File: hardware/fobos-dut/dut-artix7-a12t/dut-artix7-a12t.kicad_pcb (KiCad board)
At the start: 2 copper layers, 67 parts, among them J1 Target, J3 Vcore, J5 Conn_01x02, Q1 FDS9435A, U1 XC7A12T-CSG325, U2 SP3003-04ATG, U3 SP3003-04ATG, U4 SP3003-04ATG, U5 INA225, U6 BGA2801, U7 W25Q32JVSS

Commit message: updated 3d model path of sma connector
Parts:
- added J4: Glitch, cerg:SMA-JOHNSON-142-0701-801, F.Cu at (-147.3, 152.7)
- added J6: Measure, cerg:SMA-JOHNSON-142-0701-801, F.Cu at (-125.5, 152.4)
- moved J1 24.1 mm to (-155.7, 194.8), turned to 180 degrees
- moved U1 11.3 mm to (-97.3, 165.1)

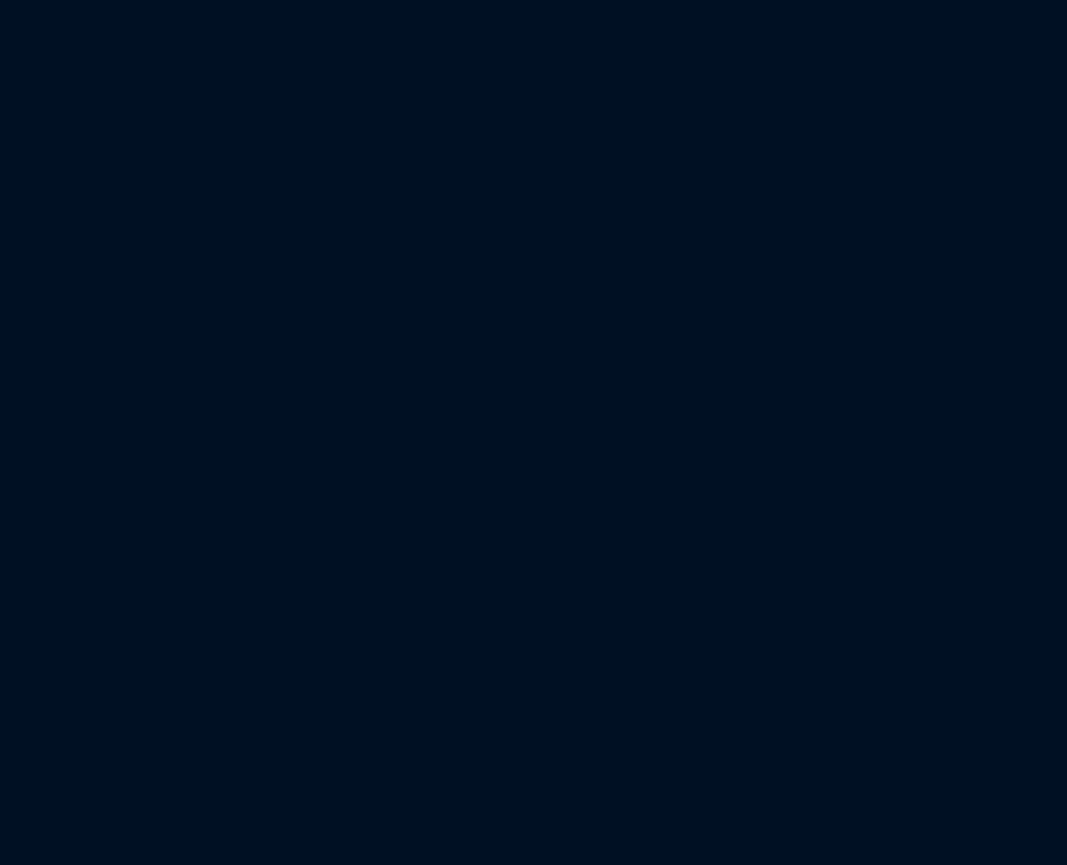
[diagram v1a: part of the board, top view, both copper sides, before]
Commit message: Finished the LTC3659 circuit - added gnd, epad to gnd net Completed PGOOD LED circuit Added slide switch to serve as ON_OFF switch
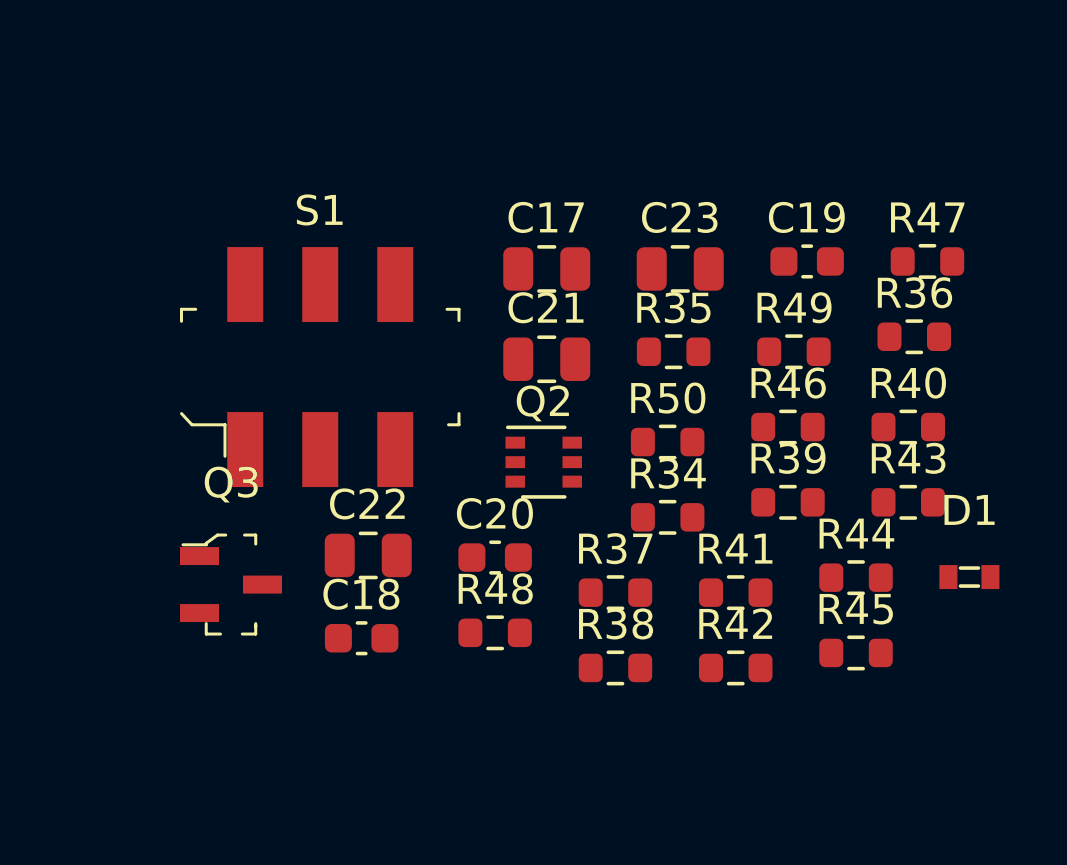
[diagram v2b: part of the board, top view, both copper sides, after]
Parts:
- added C17: 22uF, Capacitor_SMD:C_0805_2012Metric, F.Cu at (-58.3, 198.5)
- added C18: 20pF, Capacitor_SMD:C_0603_1608Metric, F.Cu at (-64.5, 210.8)
- added C19: 20pF, Capacitor_SMD:C_0603_1608Metric, F.Cu at (-49.6, 198.2)
- added C20: 20pF, Capacitor_SMD:C_0603_1608Metric, F.Cu at (-60.0, 208.1)
- added C21: 22uF, Capacitor_SMD:C_0805_2012Metric, F.Cu at (-58.3, 201.5)
- added C22: 10uF, Capacitor_SMD:C_0805_2012Metric, F.Cu at (-64.2, 208.1)
- added C23: 10uF, Capacitor_SMD:C_0805_2012Metric, F.Cu at (-53.9, 198.5)
- added D1: LG_L29K-G2J1-24-Z, digikey-footprints:0603, F.Cu at (-44.2, 208.8)
- added Q2: MBT3904DW1, Package_TO_SOT_SMD:SOT-363_SC-70-6, F.Cu at (-58.4, 204.9)
- added Q3: FDV301N, digikey-footprints:SOT-23-3, F.Cu at (-68.8, 209.0)
- added R34: 3.48KR, Resistor_SMD:R_0603_1608Metric, F.Cu at (-54.3, 206.8)
- added R35: 10KR, Resistor_SMD:R_0603_1608Metric, F.Cu at (-54.1, 201.3)
- added R36: 1KR, Resistor_SMD:R_0603_1608Metric, F.Cu at (-46.0, 200.8)
- added R37: 0, Resistor_SMD:R_0603_1608Metric, F.Cu at (-56.0, 209.3)
- added R38: 100KR, Resistor_SMD:R_0603_1608Metric, F.Cu at (-56.0, 211.8)
- added R39: 100KR, Resistor_SMD:R_0603_1608Metric, F.Cu at (-50.3, 206.3)
- added R40: 100KR, Resistor_SMD:R_0603_1608Metric, F.Cu at (-46.2, 203.8)
- added R41: 4.7KR, Resistor_SMD:R_0603_1608Metric, F.Cu at (-52.0, 209.3)
- added R42: 10KR, Resistor_SMD:R_0603_1608Metric, F.Cu at (-52.0, 211.8)
- added R43: 10KR, Resistor_SMD:R_0603_1608Metric, F.Cu at (-46.2, 206.3)
- added R44: 10KR, Resistor_SMD:R_0603_1608Metric, F.Cu at (-48.0, 208.8)
- added R45: 10KR, Resistor_SMD:R_0603_1608Metric, F.Cu at (-48.0, 211.3)
- added R46: 120KR, Resistor_SMD:R_0603_1608Metric, F.Cu at (-50.3, 203.8)
- added R47: 120KR, Resistor_SMD:R_0603_1608Metric, F.Cu at (-45.6, 198.2)
- added R48: 57.6KR, Resistor_SMD:R_0603_1608Metric, F.Cu at (-60.0, 210.6)
- added R49: 100KR, Resistor_SMD:R_0603_1608Metric, F.Cu at (-50.1, 201.3)
- added R50: 800R, Resistor_SMD:R_0603_1608Metric, F.Cu at (-54.3, 204.3)
- added S1: JS202011SCQN, digikey-footprints:Switch_Slide_JS202011SCQN, F.Cu at (-65.8, 201.8)

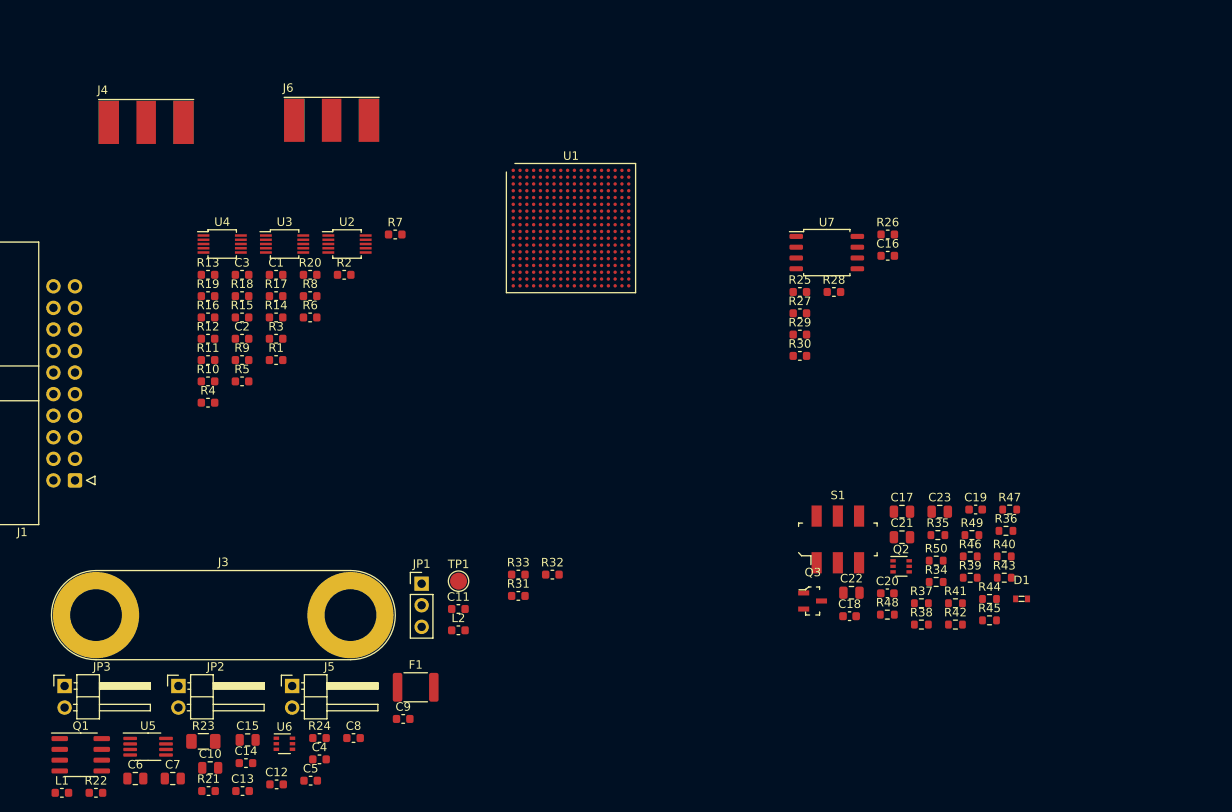
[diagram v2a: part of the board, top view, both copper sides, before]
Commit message: -Added TS3A27518EIPWRQ1 6 circuit analog SPDT switch -Connected tripple output power supply to FPGA power pins -Added bypass and decoupling capacitors to the FPGA power pins(these will be DNP) -Swapped out the old bulky banana jack socket parts for 1050752001 and 1050753001 -Added JTAG header -Added test loops -Added boot mode dip switch -Swapped out the right angle 0.1" headers for vertical 0.1" headers(personal preference) -Working my way through the 7_series_schematic_review_recommendations spreadsheet
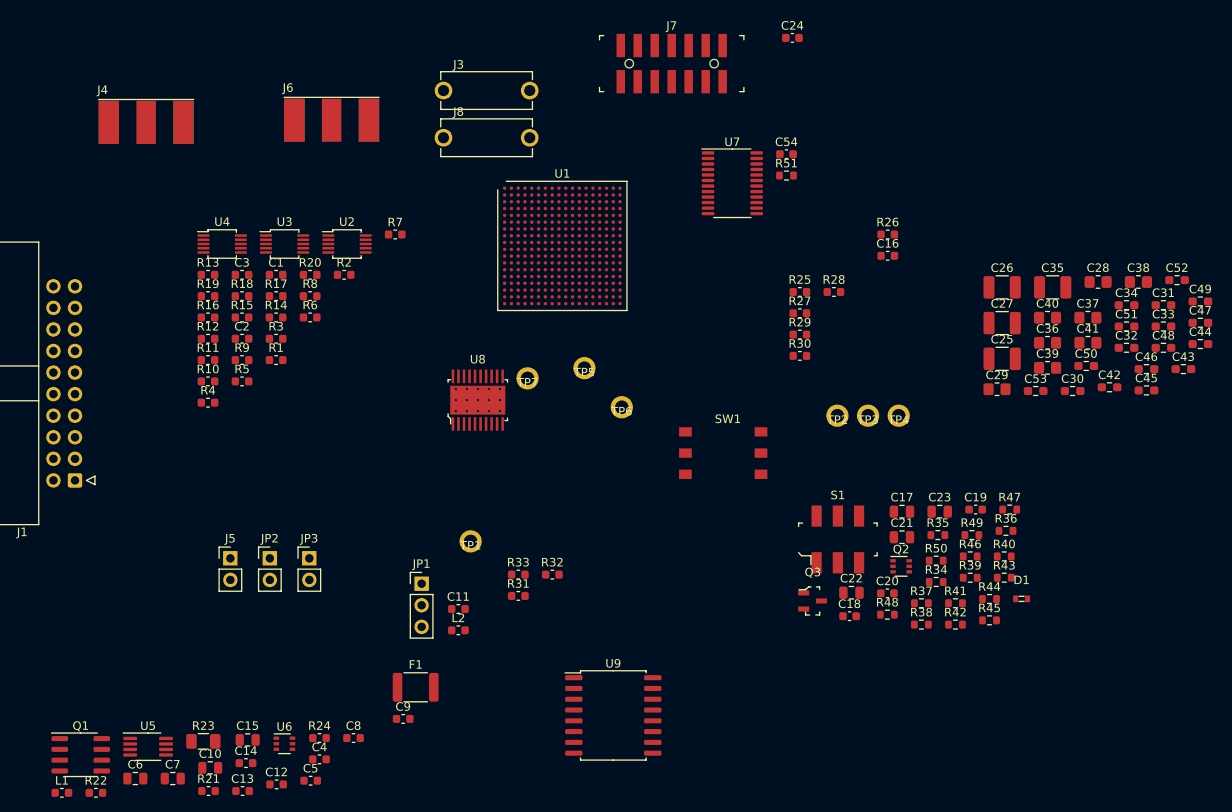
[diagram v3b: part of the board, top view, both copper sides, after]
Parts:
- added C24: 100nF, Capacitor_SMD:C_0603_1608Metric, F.Cu at (-71.2, 142.7)
- added C25: 100uF, Resistor_SMD:R_1210_3225Metric_Pad1.30x2.65mm_HandSolder, F.Cu at (-46.5, 180.5)
- added C26: 47uF, Resistor_SMD:R_1210_3225Metric_Pad1.30x2.65mm_HandSolder, F.Cu at (-46.5, 172.1)
- added C27: 47uF, Resistor_SMD:R_1210_3225Metric_Pad1.30x2.65mm_HandSolder, F.Cu at (-46.5, 176.3)
- added C28: 4.7uF, Resistor_SMD:R_0805_2012Metric_Pad1.20x1.40mm_HandSolder, F.Cu at (-35.2, 171.4)
- added C29: 4.7uF, Resistor_SMD:R_0805_2012Metric_Pad1.20x1.40mm_HandSolder, F.Cu at (-47.1, 184.1)
- added C30: .47uF, Resistor_SMD:R_0603_1608Metric_Pad0.98x0.95mm_HandSolder, F.Cu at (-38.2, 184.3)
- added C31: .47uF, Resistor_SMD:R_0603_1608Metric_Pad0.98x0.95mm_HandSolder, F.Cu at (-27.5, 174.2)
- added C32: .47uF, Resistor_SMD:R_0603_1608Metric_Pad0.98x0.95mm_HandSolder, F.Cu at (-31.9, 179.2)
- added C33: .47uF, Resistor_SMD:R_0603_1608Metric_Pad0.98x0.95mm_HandSolder, F.Cu at (-27.5, 176.7)
- added C34: .47uF, Resistor_SMD:R_0603_1608Metric_Pad0.98x0.95mm_HandSolder, F.Cu at (-31.9, 174.2)
- added C35: 47uF, Resistor_SMD:R_1210_3225Metric_Pad1.30x2.65mm_HandSolder, F.Cu at (-40.5, 172.1)
- added C36: 4.7uF, Resistor_SMD:R_0805_2012Metric_Pad1.20x1.40mm_HandSolder, F.Cu at (-41.1, 178.6)
- added C37: 4.7uF, Resistor_SMD:R_0805_2012Metric_Pad1.20x1.40mm_HandSolder, F.Cu at (-36.4, 175.7)
- added C38: 4.7uF, Resistor_SMD:R_0805_2012Metric_Pad1.20x1.40mm_HandSolder, F.Cu at (-30.4, 171.4)
- added C39: 4.7uF, Resistor_SMD:R_0805_2012Metric_Pad1.20x1.40mm_HandSolder, F.Cu at (-41.1, 181.6)
- added C40: 4.7uF, Resistor_SMD:R_0805_2012Metric_Pad1.20x1.40mm_HandSolder, F.Cu at (-41.1, 175.7)
- added C41: 4.7uF, Resistor_SMD:R_0805_2012Metric_Pad1.20x1.40mm_HandSolder, F.Cu at (-36.4, 178.6)
- added C42: .47uF, Resistor_SMD:R_0603_1608Metric_Pad0.98x0.95mm_HandSolder, F.Cu at (-33.9, 183.8)
- added C43: .47uF, Resistor_SMD:R_0603_1608Metric_Pad0.98x0.95mm_HandSolder, F.Cu at (-25.1, 181.7)
- added C44: .47uF, Resistor_SMD:R_0603_1608Metric_Pad0.98x0.95mm_HandSolder, F.Cu at (-23.1, 178.8)
- added C45: .47uF, Resistor_SMD:R_0603_1608Metric_Pad0.98x0.95mm_HandSolder, F.Cu at (-29.5, 184.2)
- added C46: .47uF, Resistor_SMD:R_0603_1608Metric_Pad0.98x0.95mm_HandSolder, F.Cu at (-29.5, 181.7)
- added C47: .47uF, Resistor_SMD:R_0603_1608Metric_Pad0.98x0.95mm_HandSolder, F.Cu at (-23.1, 176.2)
- added C48: .47uF, Resistor_SMD:R_0603_1608Metric_Pad0.98x0.95mm_HandSolder, F.Cu at (-27.5, 179.2)
- added C49: .47uF, Resistor_SMD:R_0603_1608Metric_Pad0.98x0.95mm_HandSolder, F.Cu at (-23.1, 173.7)
- added C50: .47uF, Resistor_SMD:R_0603_1608Metric_Pad0.98x0.95mm_HandSolder, F.Cu at (-36.6, 181.3)
- added C51: .47uF, Resistor_SMD:R_0603_1608Metric_Pad0.98x0.95mm_HandSolder, F.Cu at (-31.9, 176.7)
- added C52: .47uF, Resistor_SMD:R_0603_1608Metric_Pad0.98x0.95mm_HandSolder, F.Cu at (-25.9, 171.2)
- added C53: .47uF, Resistor_SMD:R_0603_1608Metric_Pad0.98x0.95mm_HandSolder, F.Cu at (-42.5, 184.3)
- added C54: 100nF, Capacitor_SMD:C_0603_1608Metric, F.Cu at (-71.9, 156.4)
- added J7: 0878321420, digikey-footprints:PinHeader_2x7_P2mm_SMD, F.Cu at (-85.4, 145.7)
- added J8: 1050752001, cerg:105075X001, F.Cu at (-112.3, 154.5)
- added R51: 10KR, Resistor_SMD:R_0603_1608Metric, F.Cu at (-71.9, 158.9)
- added SW1: SW_DIP_x03, cerg:DS04-254-2-03BK-SMT, F.Cu at (-83.8, 189.1)
- added TP2: 5281, cerg:5281, F.Cu at (-65.9, 187.2)
- added TP3: 5281, cerg:5281, F.Cu at (-62.3, 187.2)
- added TP4: 5281, cerg:5281, F.Cu at (-58.7, 187.2)
- added TP5: 5281, cerg:5281, F.Cu at (-95.7, 181.6)
- added TP6: 5281, cerg:5281, F.Cu at (-91.3, 186.2)
- added TP7: 5281, cerg:5281, F.Cu at (-102.4, 182.8)
- added U8: LTC3569EFE#PBF, digikey-footprints:TSSOP-20-1EP_W4.4mm, F.Cu at (-108.3, 185.4)
- added U9: IS25LP256D-JMLE, Package_SO:SOIC-16W_7.5x10.3mm_P1.27mm, F.Cu at (-92.3, 222.5)
- J3: value Vcore -> 1050753001; footprint Connector:Banana_Jack_2Pin -> cerg:105075X001
- J5, JP2, JP3: footprint Connector_PinHeader_2.54mm:PinHeader_1x02_P2.54mm_Horizontal -> Connector_PinHeader_2.54mm:PinHeader_1x02_P2.54mm_Vertical
- TP1: value 5V -> 5281; footprint TestPoint:TestPoint_Pad_D2.0mm -> cerg:5281
- U7: value W25Q32JVSS -> TS3A27518EIPWRQ1; footprint Package_SO:SOIC-8_5.23x5.23mm_P1.27mm -> Package_SO:TSSOP-24_4.4x7.8mm_P0.65mm
- moved J3 74.1 mm to (-112.3, 148.9)
- moved JP3 32.5 mm to (-128.1, 204.0)
- moved JP2 18.5 mm to (-132.8, 204.0)
- moved J5 16.7 mm to (-137.4, 204.0)
- moved U7 13.8 mm to (-78.3, 159.8)
- moved TP1 4.90 mm to (-109.1, 202.0)
- moved U1 2.33 mm to (-98.3, 167.2)
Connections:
- net /Connectors, IO/CV_RST renamed /Connectors, IO/CW_RST
- net /FPGA Power and Programming/FPGA_CCLK renamed /FPGA 1/FPGA_CCLK
- net CLK_C2D renamed FC2D_CLK
- net CLK_D2C renamed FD2C_CLK
- net FS_5V renamed FC_5V
- net IO renamed FC_IO
- net Net-(U5-Pad4) renamed VCORE_CURRENT
- net Net-(U5-Pad5) renamed VCORE_CURRENT_GAIN_0
- net Net-(U5-Pad6) renamed VCORE_CURRENT_GAIN_1
- net RST renamed FC_RST
- C1 pad 2: CW_VREF -> FC_3V3
- C16 pad 1: VCC -> +1V0
- C19 pad 1: +1V8 -> +1V0
- C2 pad 2: CW_VREF -> FC_3V3
- C20 pad 1: +3V3 -> +1V0
- C22 pad 1: +1V8 -> +1V0
- C23 pad 1: +3V3 -> +1V0
- C3 pad 2: CW_VREF -> FC_3V3
- D1 pad 1: CW_VREF -> FC_3V3
- J1 pad 18: CW_VREF -> FC_3V3
- J1 pad 3: CW_VREF -> FC_3V3
- J1 pad 8: CW_VREF -> FC_3V3
- J4 pad 1: VCC -> +1V0
- J5 pad 1: VCC -> +1V0
- JP1 pad 3: Net-(J3-Pad2) -> Net-(J8-Pad1)
- JP3 pad 2: VCC -> +1V0
- L2 pad 1: CW_VREF -> FC_3V3
- R15 pad 1: DIO0 -> FC_DIO0
- R16 pad 1: DIO1 -> FC_DIO1
- R17 pad 1: DIO2 -> FC_DIO2
- R18 pad 1: DIO3 -> FC_DIO3
- R23 pad 1: VCC -> +1V0
- R24 pad 2: VCC -> +1V0
- R25 pad 2: VCC -> +1V0
- R3 pad 2: TF -> FD_TF
- R31 pad 1: VCC -> +1V0
- R32 pad 1: VCC -> +1V0
- R33 pad 1: VCC -> +1V0
- R34 pad 2: +1V8 -> +1V0
- R4 pad 2: Ready -> FC2D_HS
- R44 pad 2: +1V8 -> +1V0
- R45 pad 2: +3V3 -> +1V0
- R49 pad 1: CW_VREF -> FC_3V3
- R5 pad 2: Valid -> FD2C_HS
- R6 pad 2: Aux -> FC_PROG
- U1 pad A1: Net-(U1-PadA1) -> GND
- U1 pad A11: Net-(U1-PadA1) -> GND
- U1 pad A16: Net-(U1-PadA16) -> +1V0
- U1 pad A18: Net-(U1-PadA1) -> GND
- U1 pad A2: Net-(U1-PadA2) -> GND
- U1 pad A5: Net-(U1-PadA1) -> GND
- U1 pad A7: Net-(U1-PadA1) -> GND
- U1 pad A8: Net-(U1-PadA1) -> GND
- U1 pad B13: Net-(U1-PadA16) -> +1V0
- U1 pad B18: Net-(U1-PadA1) -> GND
- U1 pad B3: Net-(U1-PadA1) -> GND
- U1 pad B4: Net-(U1-PadB4) -> GND
- U1 pad B7: Net-(U1-PadA1) -> GND
- U1 pad B8: Net-(U1-PadA1) -> GND
- U1 pad C1: Net-(U1-PadA2) -> GND
- U1 pad C10: Net-(U1-PadA16) -> +1V0
- U1 pad C15: Net-(U1-PadA1) -> GND
- U1 pad C2: Net-(U1-PadA1) -> GND
- U1 pad C5: Net-(U1-PadB4) -> GND
- U1 pad C6: Net-(U1-PadA1) -> GND
- U1 pad C7: Net-(U1-PadA1) -> GND
- U1 pad D12: Net-(U1-PadA1) -> GND
- U1 pad D17: Net-(U1-PadA16) -> +1V0
- U1 pad D3: Net-(U1-PadA1) -> GND
- U1 pad D4: Net-(U1-PadA1) -> GND
- U1 pad D7: Net-(U1-PadA1) -> GND
- U1 pad E1: Net-(U1-PadA2) -> GND
- U1 pad E10: Net-(U1-PadE10) -> +1V0
- U1 pad E11: Net-(U1-PadE11) -> GND
- U1 pad E12: Net-(U1-PadE12) -> +1V0
- U1 pad E14: Net-(U1-PadA16) -> +1V0
- U1 pad E2: Net-(U1-PadA1) -> GND
- U1 pad E5: Net-(U1-PadB4) -> GND
- U1 pad E6: Net-(U1-PadA1) -> GND
- U1 pad E7: Net-(U1-PadA1) -> GND
- U1 pad E9: Net-(U1-PadA1) -> GND
- U1 pad F10: Net-(U1-PadA1) -> GND
- U1 pad F11: Net-(U1-PadF11) -> +1V0
- U1 pad F16: Net-(U1-PadA1) -> GND
- U1 pad F3: Net-(U1-PadA2) -> GND
- U1 pad F4: Net-(U1-PadA1) -> GND
- U1 pad F5: Net-(U1-PadB4) -> GND
- U1 pad F6: Net-(U1-PadA1) -> GND
- U1 pad F7: Net-(U1-PadF7) -> +1V0
- U1 pad F9: Net-(U1-PadF7) -> +1V0
- U1 pad G1: Net-(U1-PadA1) -> GND
- U1 pad G10: Net-(U1-PadF11) -> +1V0
- U1 pad G11: Net-(U1-PadA1) -> GND
- U1 pad G12: Net-(U1-PadG12) -> +1V0
- U1 pad G13: Net-(U1-PadA1) -> GND
- U1 pad G18: Net-(U1-PadA16) -> +1V0
- U1 pad G2: Net-(U1-PadA2) -> GND
- U1 pad G5: Net-(U1-PadA1) -> GND
- U1 pad G6: Net-(U1-PadA1) -> GND
- U1 pad G7: Net-(U1-PadA1) -> GND
- U1 pad G8: Net-(U1-PadF7) -> +1V0
- U1 pad G9: Net-(U1-PadA1) -> GND
- U1 pad H10: Net-(U1-PadA1) -> GND
- U1 pad H11: Net-(U1-PadF11) -> +1V0
- U1 pad H12: Net-(U1-PadA1) -> GND
- U1 pad H13: Net-(U1-PadG12) -> +1V0
- U1 pad H15: Net-(U1-PadA16) -> +1V0
- U1 pad H3: Net-(U1-PadA1) -> GND
- U1 pad H4: Net-(U1-PadA1) -> GND
- U1 pad H5: Net-(U1-PadA1) -> GND
- U1 pad H6: Net-(U1-PadA1) -> GND
- U1 pad H7: Net-(U1-PadF7) -> +1V0
- U1 pad H8: Net-(U1-PadA1) -> GND
- U1 pad H9: Net-(U1-PadF7) -> +1V0
- U1 pad J1: Net-(U1-PadA1) -> GND
- U1 pad J10: Net-(U1-PadJ10) -> +1V0
- U1 pad J11: Net-(U1-PadA1) -> GND
- U1 pad J12: Net-(U1-PadF7) -> +1V0
- U1 pad J13: Net-(U1-PadA1) -> GND
- U1 pad J17: Net-(U1-PadA1) -> GND
- U1 pad J2: Net-(U1-PadA1) -> GND
- U1 pad J3: Net-(U1-PadA1) -> GND
- U1 pad J7: Net-(U1-PadA1) -> GND
- U1 pad J8: Net-(U1-PadF7) -> +1V0
- U1 pad J9: Net-(U1-PadJ9) -> GND
- U1 pad K10: Net-(U1-PadK10) -> GND
- U1 pad K11: Net-(U1-PadF7) -> +1V0
- U1 pad K12: Net-(U1-PadA1) -> GND
- U1 pad K13: Net-(U1-PadG12) -> +1V0
- U1 pad K14: Net-(U1-PadA1) -> GND
- U1 pad K4: Net-(U1-PadA1) -> GND
- U1 pad K7: Net-(U1-PadF7) -> +1V0
- U1 pad K8: Net-(U1-PadA1) -> GND
- U1 pad K9: Net-(U1-PadK9) -> GND
- U1 pad L1: Net-(U1-PadA1) -> GND
- U1 pad L10: Net-(U1-PadL10) -> GND
- U1 pad L11: Net-(U1-PadA1) -> GND
- U1 pad L12: Net-(U1-PadF7) -> +1V0
- U1 pad L13: Net-(U1-PadA1) -> GND
- U1 pad L16: Net-(U1-PadL16) -> +1V0
- U1 pad L6: Net-(U1-PadL6) -> +1V0
- U1 pad L7: Net-(U1-PadA1) -> GND
- U1 pad L8: Net-(U1-PadF7) -> +1V0
- U1 pad L9: Net-(U1-PadL9) -> GND
- U1 pad M10: Net-(U1-PadM10) -> GND
- U1 pad M11: Net-(U1-PadF7) -> +1V0
- U1 pad M12: Net-(U1-PadA1) -> GND
- U1 pad M13: Net-(U1-PadG12) -> +1V0
- U1 pad M18: Net-(U1-PadA1) -> GND
- U1 pad M3: Net-(U1-PadL6) -> +1V0
- U1 pad M7: Net-(U1-PadF7) -> +1V0
- U1 pad M8: Net-(U1-PadA1) -> GND
- U1 pad M9: Net-(U1-PadM9) -> GND
- U1 pad N10: Net-(U1-PadF7) -> +1V0
- U1 pad N11: Net-(U1-PadA1) -> GND
- U1 pad N12: Net-(U1-PadF7) -> +1V0
- U1 pad N13: Net-(U1-PadA1) -> GND
- U1 pad N15: Net-(U1-PadA1) -> GND
- U1 pad N5: Net-(U1-PadA1) -> GND
- U1 pad N7: Net-(U1-PadA1) -> GND
- U1 pad N8: Net-(U1-PadF7) -> +1V0
- U1 pad N9: Net-(U1-PadA1) -> GND
- U1 pad P11: Net-(U1-PadF7) -> +1V0
- U1 pad P12: Net-(U1-PadA1) -> GND
- U1 pad P13: Net-(U1-PadG12) -> +1V0
- U1 pad P17: Net-(U1-PadL16) -> +1V0
- U1 pad P2: Net-(U1-PadA1) -> GND
- U1 pad P7: Net-(U1-PadL6) -> +1V0
- U1 pad P8: Net-(U1-PadA1) -> GND
- U1 pad P9: Net-(U1-PadF7) -> +1V0
- U1 pad R10: Net-(U1-PadE10) -> +1V0
- U1 pad R14: Net-(U1-PadL16) -> +1V0
- U1 pad R4: Net-(U1-PadL6) -> +1V0
- U1 pad R9: Net-(U1-PadA1) -> GND
- U1 pad T1: Net-(U1-PadL6) -> +1V0
- U1 pad T11: Net-(U1-PadL16) -> +1V0
- U1 pad T16: Net-(U1-PadA1) -> GND
- U1 pad T6: Net-(U1-PadA1) -> GND
- U1 pad U13: Net-(U1-PadA1) -> GND
- U1 pad U18: Net-(U1-PadL16) -> +1V0
- U1 pad U3: Net-(U1-PadA1) -> GND
- U1 pad U8: Net-(U1-PadL16) -> +1V0
- U1 pad V1: Net-(U1-PadA1) -> GND
- U1 pad V10: Net-(U1-PadA1) -> GND
- U1 pad V15: Net-(U1-PadL16) -> +1V0
- U1 pad V18: Net-(U1-PadA1) -> GND
- U1 pad V5: Net-(U1-PadL6) -> +1V0
- U2 pad 1: Ready -> (Ready)FC2D_HS
- U2 pad 10: Ready -> (Ready)FC2D_HS
- U2 pad 2: DIO2 -> FC_DIO2
- U2 pad 3: CW_VREF -> FC_3V3
- U2 pad 4: Valid -> (Valid)FD2C_HS
- U2 pad 5: DIO3 -> FC_DIO3
- U2 pad 6: DIO3 -> FC_DIO3
- U2 pad 7: Valid -> (Valid)FD2C_HS
- U2 pad 9: DIO2 -> FC_DIO2
- U3 pad 3: CW_VREF -> FC_3V3
- U3 pad 4: DIO0 -> FC_DIO0
- U3 pad 5: DIO1 -> FC_DIO1
- U3 pad 6: DIO1 -> FC_DIO1
- U3 pad 7: DIO0 -> FC_DIO0
- U4 pad 3: CW_VREF -> FC_3V3
- U4 pad 4: TF -> FD_TF
- U4 pad 5: Aux -> (Aux)FC_PROG
- U4 pad 6: Aux -> (Aux)FC_PROG
- U4 pad 7: TF -> FD_TF
- U5 pad 1: Net-(U5-Pad1) -> Net-(JP2-Pad2)
- U5 pad 2: Net-(U5-Pad2) -> GND
- U5 pad 3: Net-(U5-Pad3) -> FC_3V3
- U5 pad 7: Net-(U5-Pad7) -> GND
- U5 pad 8: Net-(U5-Pad8) -> +1V0
- U7 pad 1: Net-(R25-Pad1) -> FC_DIO0_MUX
- U7 pad 2: Net-(R28-Pad2) -> Net-(U7-Pad2)
- U7 pad 3: VCC -> Net-(U7-Pad3)
- U7 pad 4: GND -> FD_TF
- U7 pad 5: Net-(R27-Pad2) -> GND
- U7 pad 6: Net-(R26-Pad1) -> FC_DIO0
- U7 pad 7: VCC -> FC_DIO1
- U7 pad 8: VCC -> FC_3V3
